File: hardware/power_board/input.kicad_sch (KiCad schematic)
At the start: 11 parts, among them J2 12 V ACC in

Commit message: PCBs routed, labelled and ready to order: Rev 1 fabrication files and buy list
Both boards placed, routed and finished by script (hardware/gen): layout.sh places
(placement.py, with silkscreen names for every terminal, port, header and button),
route.sh routes with Freerouting inside rule areas and net classes from the layout
guide and keeps a board only with 0 DRC errors, 0 unconnected and exact schematic
parity, routespec.sh checks what the DRC cannot (planes, crystal, converter loop,
IPC-2221 widths), finish.sh adds the bottom-silkscreen identification and writes
the fabrication files (gerbers, drill, BOM, positions) only when the DRC passes.

- Pod 70 x 53 mm, 4 layers: In1 solid GND, In2 +3V3, 530 teardrops; no DRC warnings.
- Power 95 x 66 mm, 2 layers, 2 oz: 10 A rail as a zone, converter re-placed (switch
  node 16 mm, feedback 7 mm, no vias; was 78 mm and 40 mm), 328 teardrops.
- Screw terminals turned to open outward; RESET/BOOT side-push on the pod's left
  edge; USB-C footprint with a 3D model (GCT USB4105).
- Pod J2 now the Adafruit 4754's JP1 row pin for pin (the old order shorted its
  3.3 V output to ground); IMU reset on a new J8; HC-05 header fed 5 V.
- Buy list per footprint and module connections in bill-of-materials.md section 10.
- LAYOUT_GUIDE rewritten as how the boards were routed and how to review them;
  decisions, progress log and BUILD_GUIDE updated; power box follows the wider board.
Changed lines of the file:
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@@
 		(instances
 			(project "power_board"
-				(path "/244ac675-494c-4e27-8819-02215b480bc3/6e2425bd-7906-41e3-a52a-98bd4c9fedd6"
+				(path "/c794bf93-11d2-4d5c-a02b-6bb49c306097/12d85e82-abe0-4648-bbe9-6ecece6cffd7"
 					(reference "J2")
 					(unit 1)
@@
 		(instances
 			(project "power_board"
-				(path "/244ac675-494c-4e27-8819-02215b480bc3/6e2425bd-7906-41e3-a52a-98bd4c9fedd6"
+				(path "/c794bf93-11d2-4d5c-a02b-6bb49c306097/12d85e82-abe0-4648-bbe9-6ecece6cffd7"
 					(reference "F1")
 					(unit 1)
@@
 		(instances
 			(project "power_board"
-				(path "/244ac675-494c-4e27-8819-02215b480bc3/6e2425bd-7906-41e3-a52a-98bd4c9fedd6"
+				(path "/c794bf93-11d2-4d5c-a02b-6bb49c306097/12d85e82-abe0-4648-bbe9-6ecece6cffd7"
 					(reference "D10")
 					(unit 1)
@@
 		(instances
 			(project "power_board"
-				(path "/244ac675-494c-4e27-8819-02215b480bc3/6e2425bd-7906-41e3-a52a-98bd4c9fedd6"
+				(path "/c794bf93-11d2-4d5c-a02b-6bb49c306097/12d85e82-abe0-4648-bbe9-6ecece6cffd7"
 					(reference "D11")
 					(unit 1)
@@
 		(instances
 			(project "power_board"
-				(path "/244ac675-494c-4e27-8819-02215b480bc3/6e2425bd-7906-41e3-a52a-98bd4c9fedd6"
+				(path "/c794bf93-11d2-4d5c-a02b-6bb49c306097/12d85e82-abe0-4648-bbe9-6ecece6cffd7"
 					(reference "C20")
 					(unit 1)
@@
 		(instances
 			(project "power_board"
-				(path "/244ac675-494c-4e27-8819-02215b480bc3/6e2425bd-7906-41e3-a52a-98bd4c9fedd6"
+				(path "/c794bf93-11d2-4d5c-a02b-6bb49c306097/12d85e82-abe0-4648-bbe9-6ecece6cffd7"
 					(reference "R40")
 					(unit 1)
@@
 		(instances
 			(project "power_board"
-				(path "/244ac675-494c-4e27-8819-02215b480bc3/6e2425bd-7906-41e3-a52a-98bd4c9fedd6"
+				(path "/c794bf93-11d2-4d5c-a02b-6bb49c306097/12d85e82-abe0-4648-bbe9-6ecece6cffd7"
 					(reference "D12")
 					(unit 1)
@@
 		(instances
 			(project "power_board"
-				(path "/244ac675-494c-4e27-8819-02215b480bc3/6e2425bd-7906-41e3-a52a-98bd4c9fedd6"
+				(path "/c794bf93-11d2-4d5c-a02b-6bb49c306097/12d85e82-abe0-4648-bbe9-6ecece6cffd7"
 					(reference "H1")
 					(unit 1)
@@
 		(instances
 			(project "power_board"
-				(path "/244ac675-494c-4e27-8819-02215b480bc3/6e2425bd-7906-41e3-a52a-98bd4c9fedd6"
+				(path "/c794bf93-11d2-4d5c-a02b-6bb49c306097/12d85e82-abe0-4648-bbe9-6ecece6cffd7"
 					(reference "H2")
 					(unit 1)
@@
 		(instances
 			(project "power_board"
-				(path "/244ac675-494c-4e27-8819-02215b480bc3/6e2425bd-7906-41e3-a52a-98bd4c9fedd6"
+				(path "/c794bf93-11d2-4d5c-a02b-6bb49c306097/12d85e82-abe0-4648-bbe9-6ecece6cffd7"
 					(reference "H3")
 					(unit 1)
@@
 		(instances
 			(project "power_board"
-				(path "/244ac675-494c-4e27-8819-02215b480bc3/6e2425bd-7906-41e3-a52a-98bd4c9fedd6"
+				(path "/c794bf93-11d2-4d5c-a02b-6bb49c306097/12d85e82-abe0-4648-bbe9-6ecece6cffd7"
 					(reference "H4")
 					(unit 1)
@@
 		(instances
 			(project "power_board"
-				(path "/244ac675-494c-4e27-8819-02215b480bc3/6e2425bd-7906-41e3-a52a-98bd4c9fedd6"
+				(path "/c794bf93-11d2-4d5c-a02b-6bb49c306097/12d85e82-abe0-4648-bbe9-6ecece6cffd7"
 					(reference "#PWR001")
 					(unit 1)
@@
 		(instances
 			(project "power_board"
-				(path "/244ac675-494c-4e27-8819-02215b480bc3/6e2425bd-7906-41e3-a52a-98bd4c9fedd6"
+				(path "/c794bf93-11d2-4d5c-a02b-6bb49c306097/12d85e82-abe0-4648-bbe9-6ecece6cffd7"
 					(reference "#FLG001")
 					(unit 1)
@@
 		(instances
 			(project "power_board"
-				(path "/244ac675-494c-4e27-8819-02215b480bc3/6e2425bd-7906-41e3-a52a-98bd4c9fedd6"
+				(path "/c794bf93-11d2-4d5c-a02b-6bb49c306097/12d85e82-abe0-4648-bbe9-6ecece6cffd7"
 					(reference "#PWR002")
 					(unit 1)
@@
 		(instances
 			(project "power_board"
-				(path "/244ac675-494c-4e27-8819-02215b480bc3/6e2425bd-7906-41e3-a52a-98bd4c9fedd6"
+				(path "/c794bf93-11d2-4d5c-a02b-6bb49c306097/12d85e82-abe0-4648-bbe9-6ecece6cffd7"
 					(reference "#FLG002")
 					(unit 1)
@@
 		(instances
 			(project "power_board"
-				(path "/244ac675-494c-4e27-8819-02215b480bc3/6e2425bd-7906-41e3-a52a-98bd4c9fedd6"
+				(path "/c794bf93-11d2-4d5c-a02b-6bb49c306097/12d85e82-abe0-4648-bbe9-6ecece6cffd7"
 					(reference "#PWR003")
 					(unit 1)
@@
 		(instances
 			(project "power_board"
-				(path "/244ac675-494c-4e27-8819-02215b480bc3/6e2425bd-7906-41e3-a52a-98bd4c9fedd6"
+				(path "/c794bf93-11d2-4d5c-a02b-6bb49c306097/12d85e82-abe0-4648-bbe9-6ecece6cffd7"
 					(reference "#PWR004")
 					(unit 1)
@@
 		(instances
 			(project "power_board"
-				(path "/244ac675-494c-4e27-8819-02215b480bc3/6e2425bd-7906-41e3-a52a-98bd4c9fedd6"
+				(path "/c794bf93-11d2-4d5c-a02b-6bb49c306097/12d85e82-abe0-4648-bbe9-6ecece6cffd7"
 					(reference "#PWR005")
 					(unit 1)
@@
 		(instances
 			(project "power_board"
-				(path "/244ac675-494c-4e27-8819-02215b480bc3/6e2425bd-7906-41e3-a52a-98bd4c9fedd6"
+				(path "/c794bf93-11d2-4d5c-a02b-6bb49c306097/12d85e82-abe0-4648-bbe9-6ecece6cffd7"
 					(reference "#PWR006")
 					(unit 1)
@@
 		(instances
 			(project "power_board"
-				(path "/244ac675-494c-4e27-8819-02215b480bc3/6e2425bd-7906-41e3-a52a-98bd4c9fedd6"
+				(path "/c794bf93-11d2-4d5c-a02b-6bb49c306097/12d85e82-abe0-4648-bbe9-6ecece6cffd7"
 					(reference "#PWR007")
 					(unit 1)
@@
 	(wire
 		(pts
+			(xy 40.64 76.2)
+			(xy 41.91 76.2)
+		)
+		(stroke
+			(width 0)
+			(type default)
+		)
+	)
+	(wire
+		(pts
 			(xy 41.91 76.2)
 			(xy 62.23 76.2)
@@
 	(wire
 		(pts
-			(xy 40.64 76.2)
-			(xy 41.91 76.2)
-		)
-		(stroke
-			(width 0)
-			(type default)
-		)
-	)
-	(wire
-		(pts
-			(xy 113.03 76.2)
+			(xy 69.85 76.2)
+			(xy 71.12 76.2)
+		)
+		(stroke
+			(width 0)
+			(type default)
+		)
+	)
+	(wire
+		(pts
+			(xy 71.12 76.2)
 			(xy 91.44 76.2)
-		)
-		(stroke
-			(width 0)
-			(type default)
-		)
-	)
-	(wire
-		(pts
-			(xy 91.44 76.2)
-			(xy 71.12 76.2)
-		)
-		(stroke
-			(width 0)
-			(type default)
-		)
-	)
-	(wire
-		(pts
-			(xy 71.12 76.2)
-			(xy 69.85 76.2)
 		)
 		(stroke
@@
 			(xy 91.44 76.2)
 			(xy 91.44 85.09)
+		)
+		(stroke
+			(width 0)
+			(type default)
+		)
+	)
+	(wire
+		(pts
+			(xy 91.44 76.2)
+			(xy 113.03 76.2)
 		)
 		(stroke
@@
 	(wire
 		(pts
+			(xy 120.65 76.2)
+			(xy 146.05 76.2)
+		)
+		(stroke
+			(width 0)
+			(type default)
+		)
+	)
+	(wire
+		(pts
+			(xy 146.05 76.2)
+			(xy 146.05 78.74)
+		)
+		(stroke
+			(width 0)
+			(type default)
+		)
+	)
+	(wire
+		(pts
+			(xy 146.05 78.74)
+			(xy 147.32 78.74)
+		)
+		(stroke
+			(width 0)
+			(type default)
+		)
+	)
+	(wire
+		(pts
+			(xy 147.32 78.74)
+			(xy 147.32 80.01)
+		)
+		(stroke
+			(width 0)
+			(type default)
+		)
+	)
+	(wire
+		(pts
+			(xy 147.32 78.74)
+			(xy 172.72 78.74)
+		)
+		(stroke
+			(width 0)
+			(type default)
+		)
+	)
+	(wire
+		(pts
+			(xy 172.72 72.39)
+			(xy 172.72 78.74)
+		)
+		(stroke
+			(width 0)
+			(type default)
+		)
+	)
+	(wire
+		(pts
+			(xy 172.72 72.39)
+			(xy 193.04 72.39)
+		)
+		(stroke
+			(width 0)
+			(type default)
+		)
+	)
+	(wire
+		(pts
+			(xy 172.72 78.74)
+			(xy 172.72 80.01)
+		)
+		(stroke
+			(width 0)
+			(type default)
+		)
+	)
+	(wire
+		(pts
 			(xy 193.04 71.12)
 			(xy 193.04 72.39)
 		)
 		(stroke
-			(width 0)
-			(type default)
-		)
-	)
-	(wire
-		(pts
-			(xy 146.05 78.74)
-			(xy 146.05 76.2)
-		)
-		(stroke
-			(width 0)
-			(type default)
-		)
-	)
-	(wire
-		(pts
-			(xy 146.05 76.2)
-			(xy 120.65 76.2)
-		)
-		(stroke
-			(width 0)
-			(type default)
-		)
-	)
-	(wire
-		(pts
-			(xy 172.72 78.74)
-			(xy 147.32 78.74)
-		)
-		(stroke
-			(width 0)
-			(type default)
-		)
-	)
-	(wire
-		(pts
-			(xy 172.72 72.39)
-			(xy 193.04 72.39)
-		)
-		(stroke
-			(width 0)
-			(type default)
-		)
-	)
-	(wire
-		(pts
-			(xy 172.72 80.01)
-			(xy 172.72 78.74)
-		)
-		(stroke
-			(width 0)
-			(type default)
-		)
-	)
-	(wire
-		(pts
-			(xy 147.32 78.74)
-			(xy 147.32 80.01)
-		)
-		(stroke
-			(width 0)
-			(type default)
-		)
-	)
-	(wire
-		(pts
-			(xy 172.72 72.39)
-			(xy 172.72 78.74)
-		)
-		(stroke
-			(width 0)
-			(type default)
-		)
-	)
-	(wire
-		(pts
-			(xy 146.05 78.74)
-			(xy 147.32 78.74)
-		)
-		(stroke

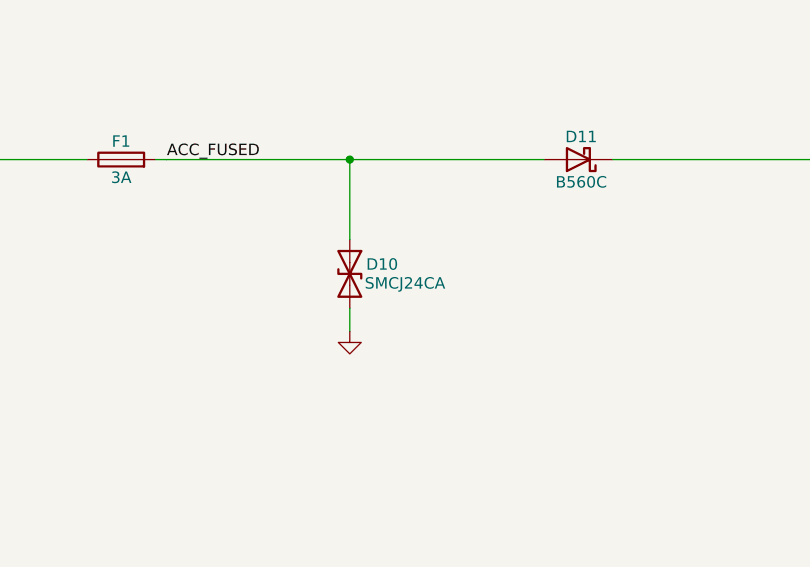
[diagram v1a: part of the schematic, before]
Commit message: TVS D10 now SMCJ33CA; 12 V input protection simulated
hardware/sim/run_input.sh simulates the power board's input (3 A fuse, TVS,
B560C reverse diode, C20) against ISO 16750-2 and ISO 7637-2 for a 12 V car:
normal running, reversed battery, 24 V jump-start, the centrally suppressed load
dump (35 V for 400 ms) and pulses 1 and 2a. The SMCJ24CA first chosen breaks
down at ~27 V, so in the suppressed load dump it tried to hold the car's whole
supply down (~100 ms at up to 141 W, near its rating). The SMCJ33CA breaks down
at ~37 V: it stays idle through that dump (rail at most 33 V; the buck, C20 and
D11 are rated 60 V or more) and still clamps the fast spikes. Same SMC
footprint: only the value changed, copper and teardrops untouched.

Also: the pod's J8 had no off-board wiring entry for the assembly documents.
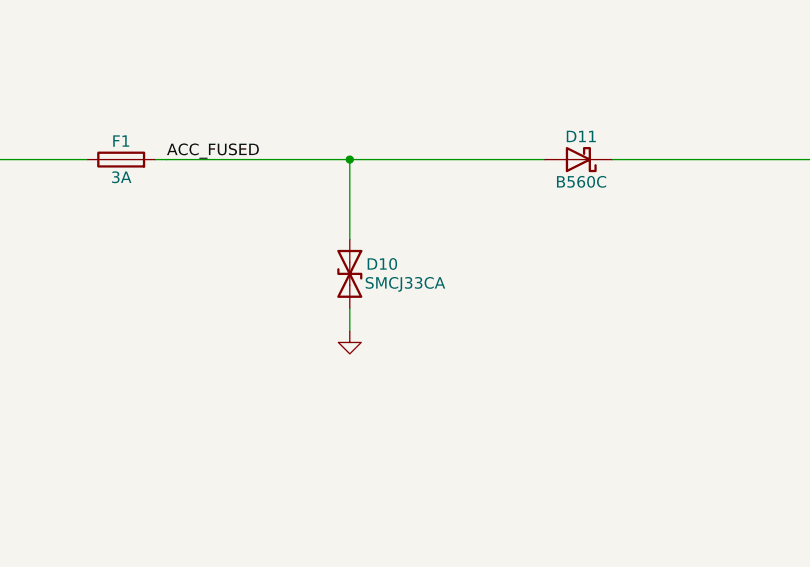
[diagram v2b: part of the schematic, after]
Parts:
- D10: value SMCJ24CA -> SMCJ33CA
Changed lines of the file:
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@@
 			)
 		)
-		(property "Value" "SMCJ24CA"
+		(property "Value" "SMCJ33CA"
 			(at 97.574 89.95 90)
 			(effects
@@
 			)
 		)
-		(property "Description" "load-dump / jump-start transient clamp (bidirectional: also survives reversed leads)"
+		(property "Description" "fast-transient clamp, above the 35 V suppressed load dump (bidirectional: survives reversed leads)"
 			(at 91.44 88.9 0)
 			(hide yes)
